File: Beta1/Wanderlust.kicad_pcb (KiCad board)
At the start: 2 copper layers, 15.2 x 17.8 mm, 26 parts, among them P0 CONN_01X01, P1 CONN_01X01, P10 CONN_01X01, P11 CONN_01X01, P2 CONN_01X01, P3 CONN_01X01, P4 CONN_01X01, P5 CONN_01X01, P6 CONN_01X01, P7 CONN_01X01, P8 CONN_01X01, P9 CONN_01X01, U1 MPR121QR2

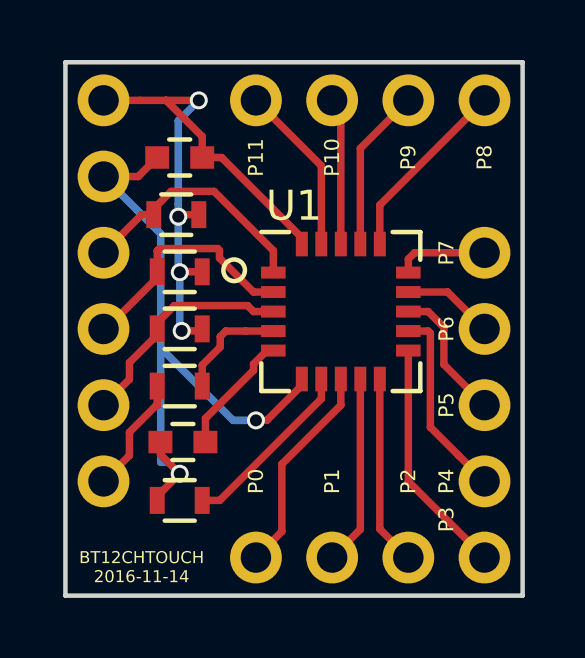
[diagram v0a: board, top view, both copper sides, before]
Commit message: Catchup Commit.  Non-atomic, Refactored LED, Keyboard, KeyPAD, and Knobs PCBs
LED: Changed chips. Cleaned up silkscreen text. Added some support
mounting holes. Shrank height of board to avoid stackup. KeyPAD is
updated with new footprint. Keyboard and Knobs are unknown.
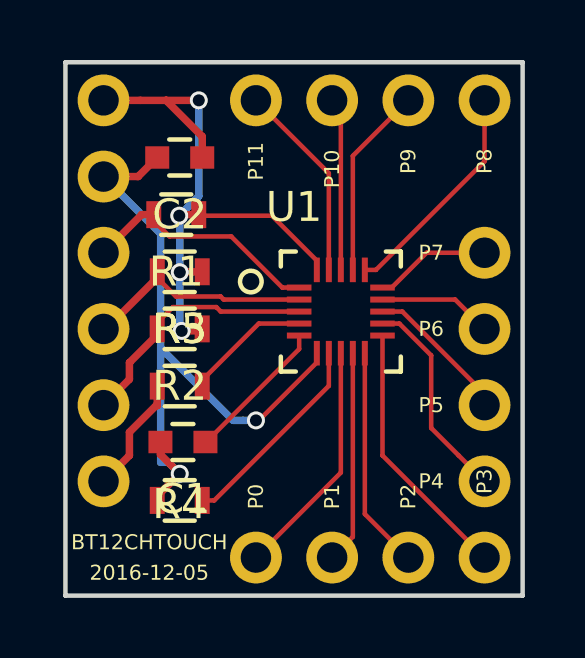
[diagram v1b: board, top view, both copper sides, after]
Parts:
- U1: footprint QFN-20-1EP_3x3mm_Pitch0.65mm -> Liberry:QFN-20-1EP_3x3mm_Pitch0.40mm
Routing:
- net /P08: track 6.24 -> 7.52 mm
- net /P02: track 6.34 -> 7.41 mm
- net /P11: track 5.69 -> 6.66 mm
- net /P09: track 5.45 -> 6.42 mm
- net GND: track 22.3 -> 23.2 mm
- net /P10: track 4.91 -> 5.77 mm
- net /P00: track 7.12 -> 7.98 mm
- net Net-(R4-Pad1): track 6.03 -> 6.89 mm
- net /P03: track 7.95 -> 8.81 mm
- net /SDA: track 7.68 -> 8.50 mm
- net /P07: track 3.08 -> 3.88 mm
- net +3V3: track 20.6 -> 21.4 mm
- net /P06: track 3.05 -> 3.81 mm
- net /P01: track 6.34 -> 7.10 mm
- net Net-(C1-Pad1): track 4.11 -> 4.86 mm
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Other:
- board text added: "2016-12-05"
- board text added: "No Hard Feelings? Try Empathy"
- board text removed: "2016-11-14"
